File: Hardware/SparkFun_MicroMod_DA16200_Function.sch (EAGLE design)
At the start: 41 parts, among them J1 MICROMOD_STANDARD, J2 CORTEX_JTAG_DEBUG, U1 DA16200MOD, U2 CH340E_MSOP10, U3 3.3V, U4 EEPROM

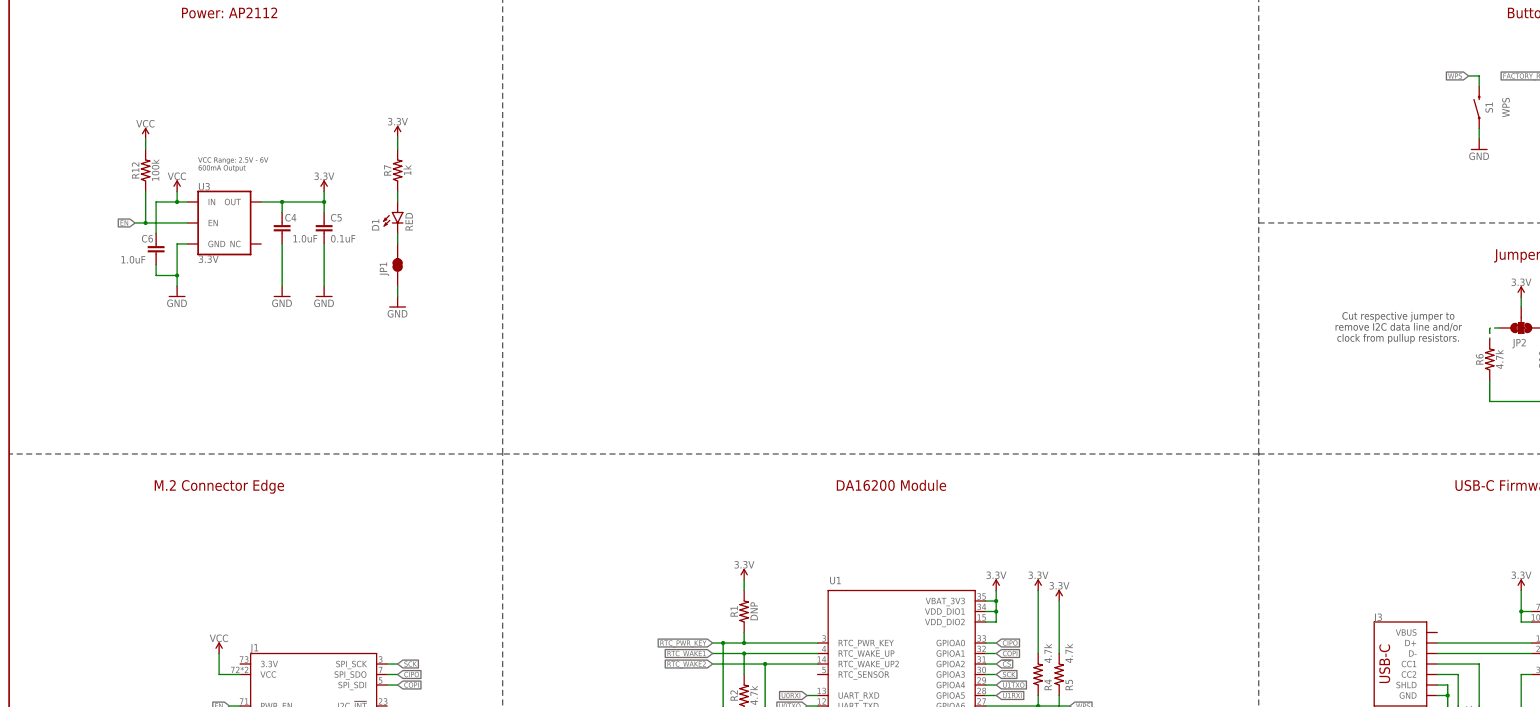
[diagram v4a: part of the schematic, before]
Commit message: V10 update
Added diodes for VIN and VUSB
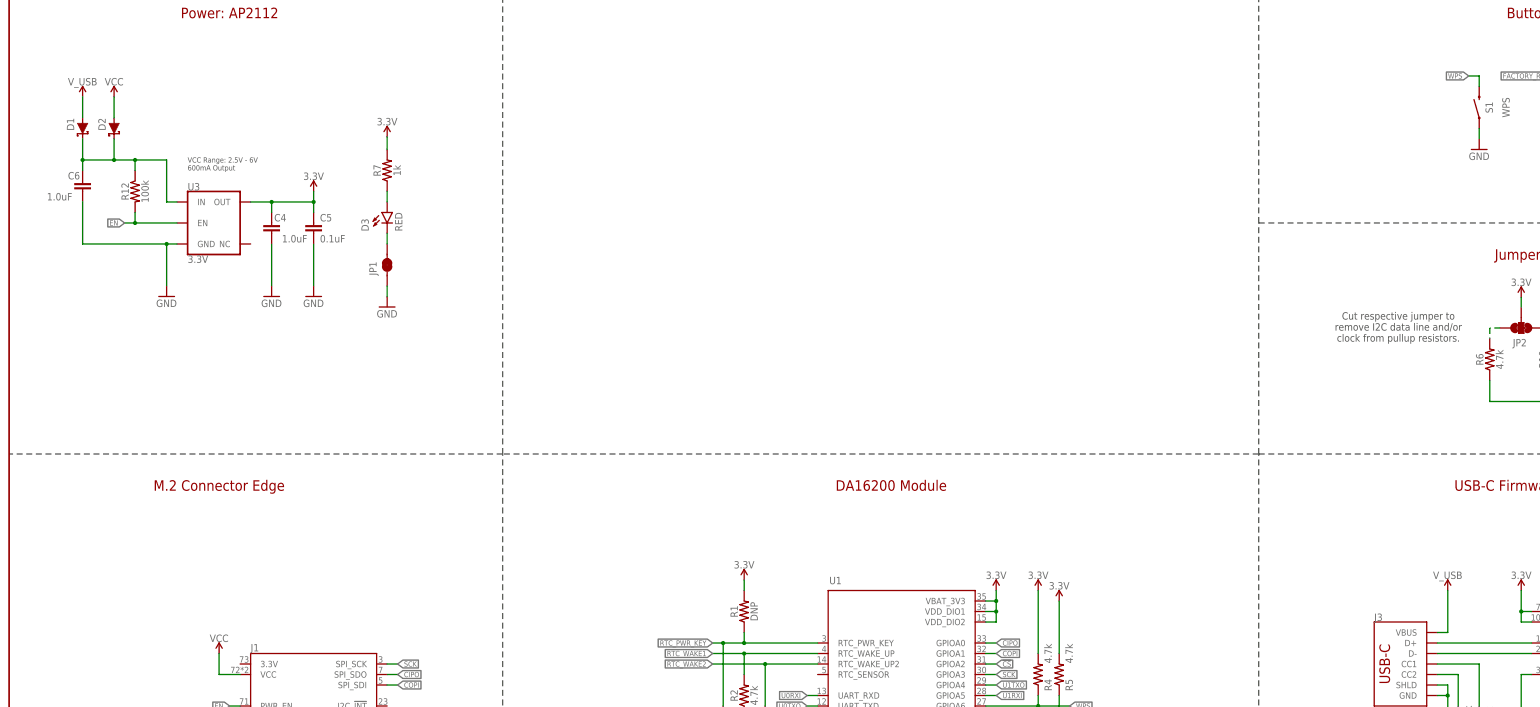
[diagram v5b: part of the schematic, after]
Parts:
- added D2: (no value), SparkFun-DiscreteSemi:DIODE-SCHOTTKY-BAT60A
- added D3: RED, SparkFun-MicroMod-Function:LED-0603_RIGHT_ANGLE
- D1: value RED -> (none); device SparkFun-MicroMod-Function:LED-0603_RIGHT_ANGLE -> SparkFun-DiscreteSemi:DIODE-SCHOTTKY-BAT60A
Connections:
- new net N$3: C6.1, D1.C, D2.C, R12.1, U3.IN
- new net V_USB: D1.A, J3.VBUS
- net EN: now also R12.2; no longer R12.1
- net N$6: now also D3.C; no longer D1.C
- net N$7: now also D3.A; no longer D1.A
- net VCC: now also D2.A; no longer C6.1, R12.2, U3.IN
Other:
- moved on the sheet: C4, C5, C6, JP1, R12, R7, U3

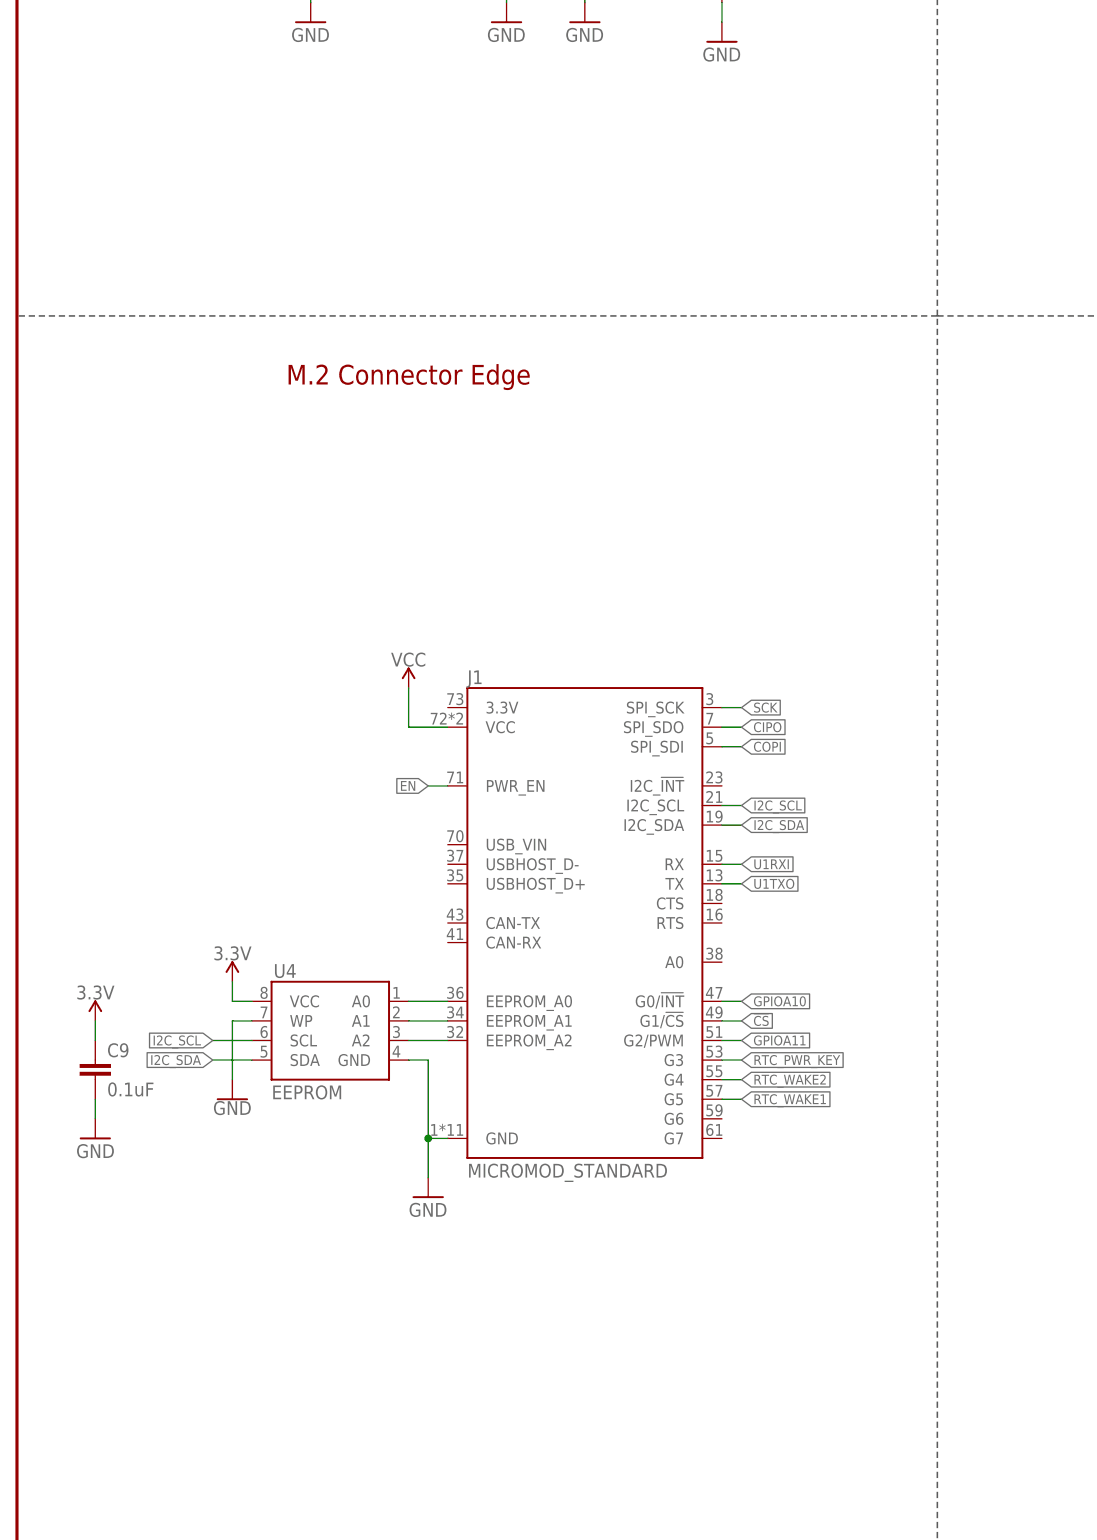
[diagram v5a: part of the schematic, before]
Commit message: V10 EEPROM changes
Added pullup, jumper, and MM pin map for EEPROM WP pin
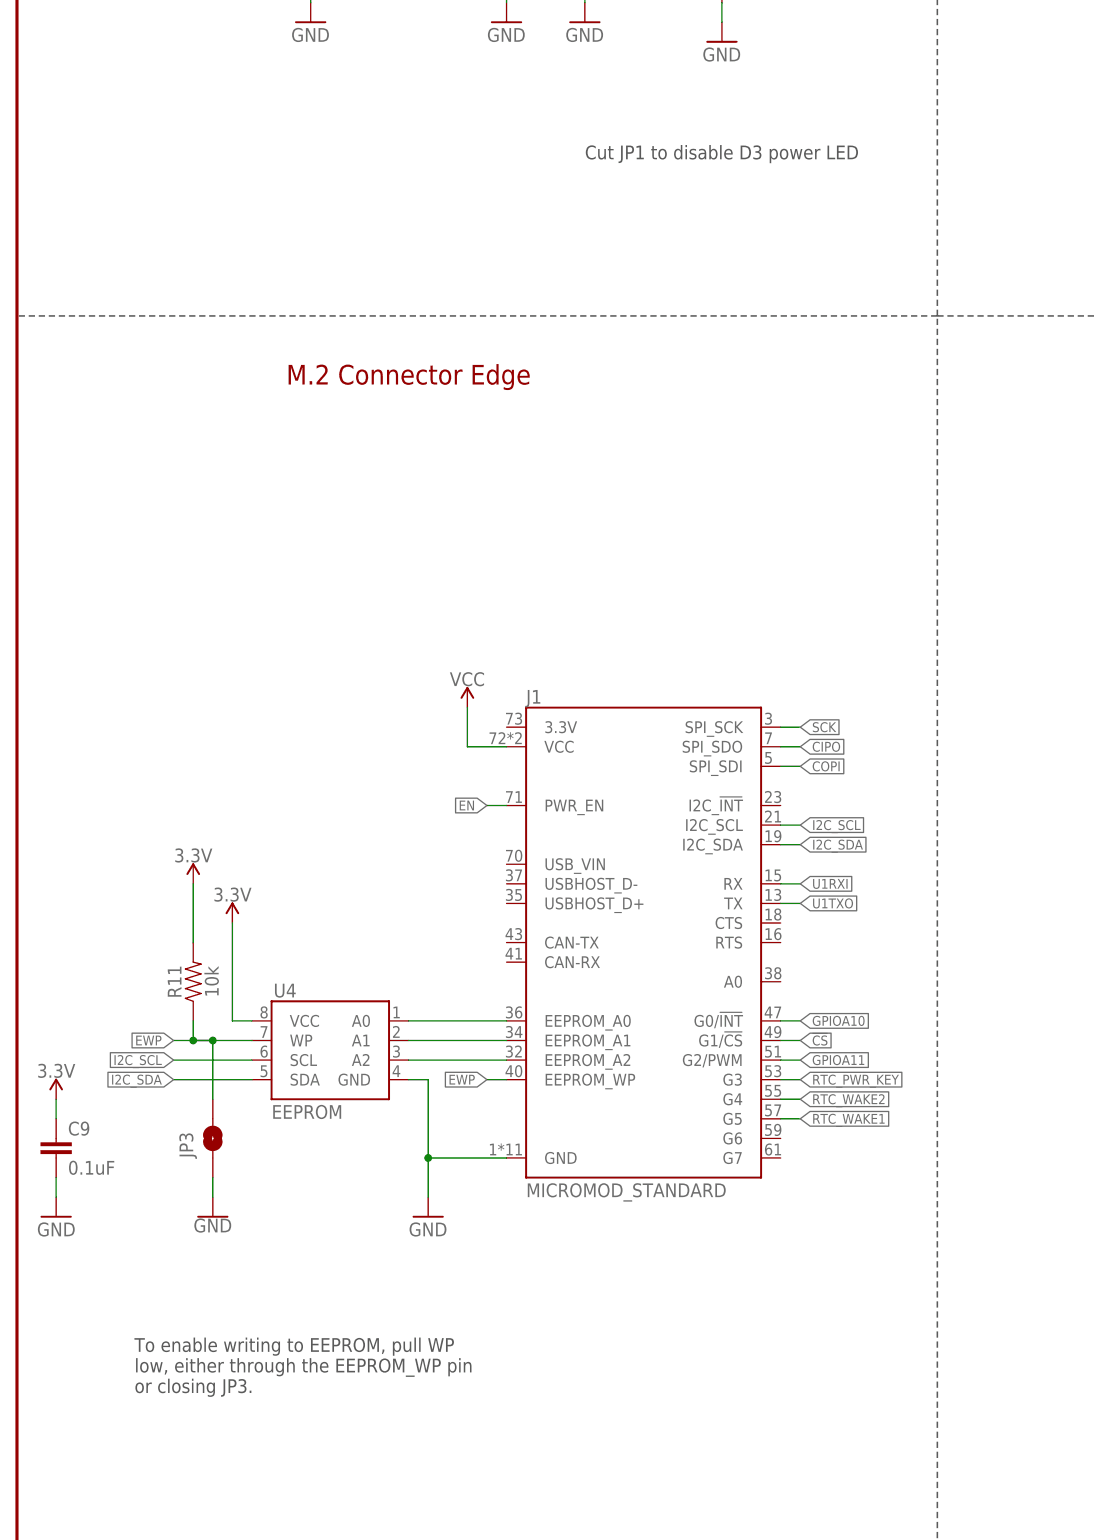
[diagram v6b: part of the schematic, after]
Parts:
- added JP3: JUMPER-SMT_2_NO_SILK, SparkFun-Jumpers:JUMPER-SMT_2_NO_SILK
- added R11: 10k, SparkFun-Resistors:10KOHM-0603-1/10W-1%
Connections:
- new net EWP: J1.EEPROM_WP, JP3.2, R11.1, U4.WP
- net 3.3V: now also R11.2
- net GND: now also JP3.1; no longer U4.WP
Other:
- note added: "Cut JP1 to disable D3 power LED"
- note added: "To enable writing to EEPROM, pull WP low, either through the EEPROM_WP pin or closing JP3."
- moved on the sheet: C9, U4

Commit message: Updates function board symbol, fixes text that was not vector
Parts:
- R1: value DNP -> (none)
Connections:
- net !CS!: now also J1.F1/!CS!; no longer J1.G1/!CS!
- net GPIOA10: now also J1.F0/!INT!; no longer J1.G0/!INT!
- net GPIOA11: now also J1.F2/PWM; no longer J1.G2/PWM
- net RTC_PWR_KEY: now also J1.F3; no longer J1.G3
- net RTC_WAKE1: now also J1.F5; no longer J1.G5
- net RTC_WAKE2: now also J1.F4; no longer J1.G4
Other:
- moved on the sheet: C1, C2, C3, C4, C5, C6, C7, C8, D1, D2, D3, J2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

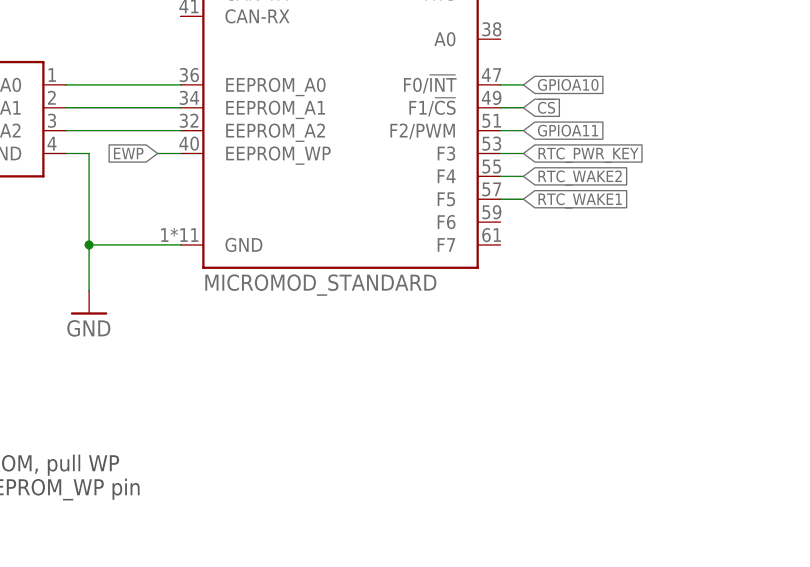
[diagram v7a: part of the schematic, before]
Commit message: Updates the design to use the Micromod-function device in the official SFE Eagle Libs
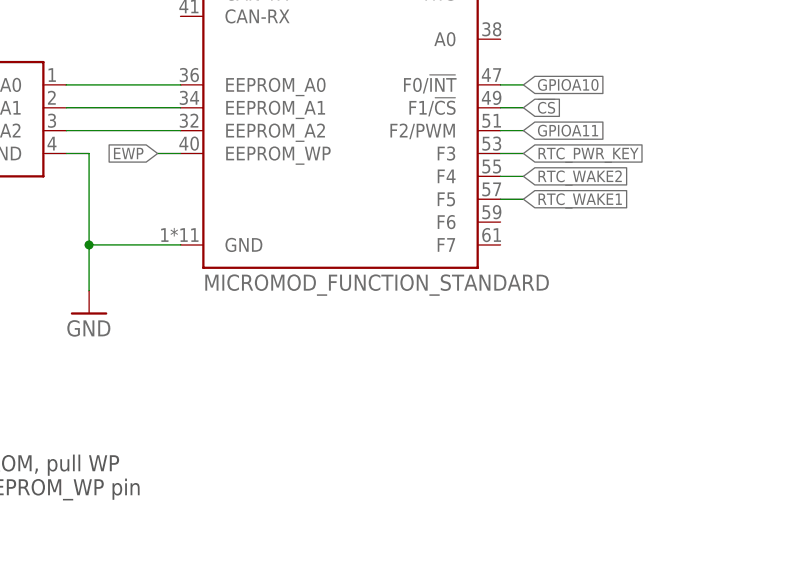
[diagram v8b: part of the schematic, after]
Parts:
- J1: value MICROMOD_STANDARD -> MICROMOD_FUNCTION_STANDARD; device SparkFun-MicroMod-Function:MICROMOD_STANDARD -> SparkFun-MicroMod:MICROMOD_FUNCTION_STANDARD
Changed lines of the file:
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@@
 <?xml version="1.0" encoding="utf-8"?>
 <!DOCTYPE eagle SYSTEM "eagle.dtd">
-<eagle version="9.6.2">
+<eagle version="9.5.1">
 <drawing>
 <settings>
@@
 </classes>
 <parts>
-<part name="J1" library="SparkFun-MicroMod-Function" deviceset="MICROMOD" device="_STANDARD"/>
+<part name="J1" library="SparkFun-MicroMod" deviceset="MICROMOD_FUNCTION" device="_STANDARD"/>
 <part name="GND11" library="SparkFun-PowerSymbols" deviceset="GND" device=""/>
 <part name="GND13" library="SparkFun-PowerSymbols" deviceset="GND" device=""/>
